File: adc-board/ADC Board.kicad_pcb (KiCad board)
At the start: 4 copper layers, 92.7 x 83.8 mm, 123 parts, among them J1 BHR-44-HUA, J10 BootJumper, J11 USB Header, J2 ST-LINK/V2, J3 USART3, J4 USART1, J5 UE27AC5410H, J6 54601-908WPLF, J7 AltPowerInput, J8 USBPowerJumper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

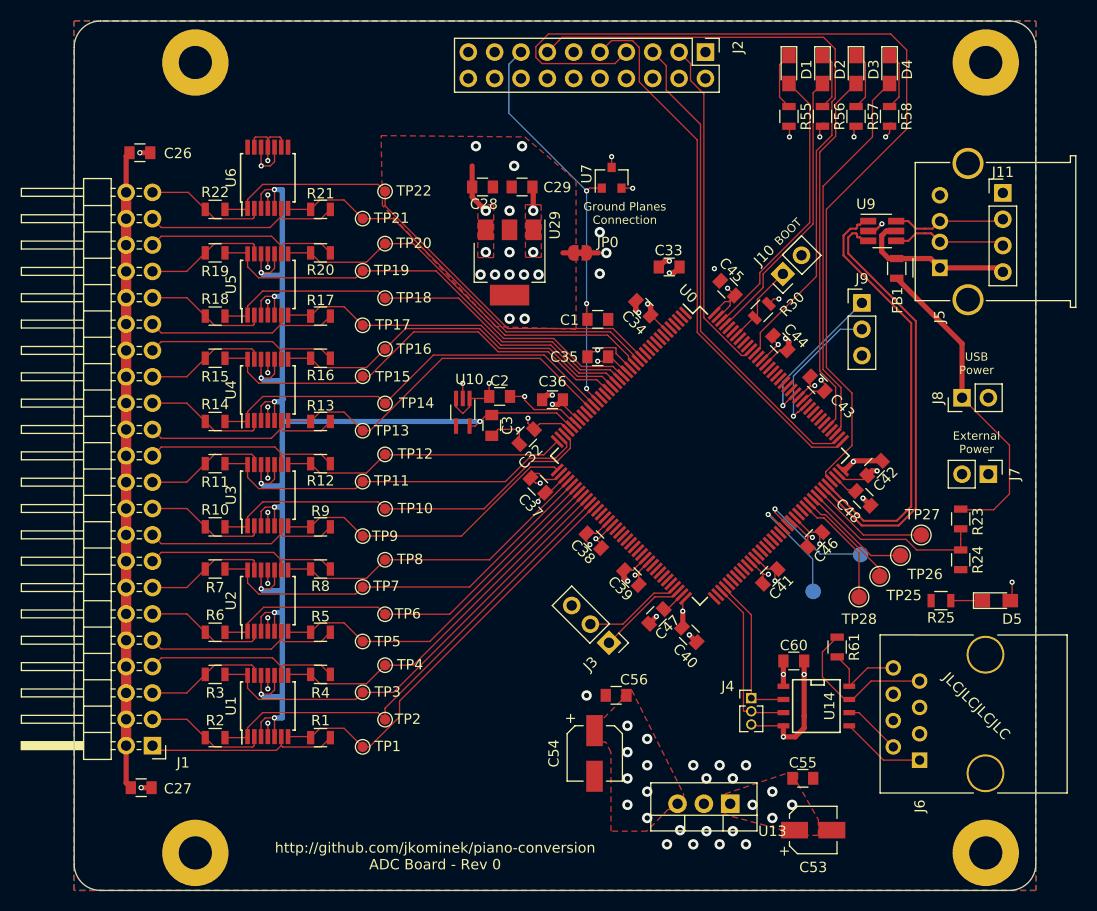
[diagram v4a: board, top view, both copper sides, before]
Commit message: Swap USART1 and USART3 on RS485 connection, so that main board has bootloader access.
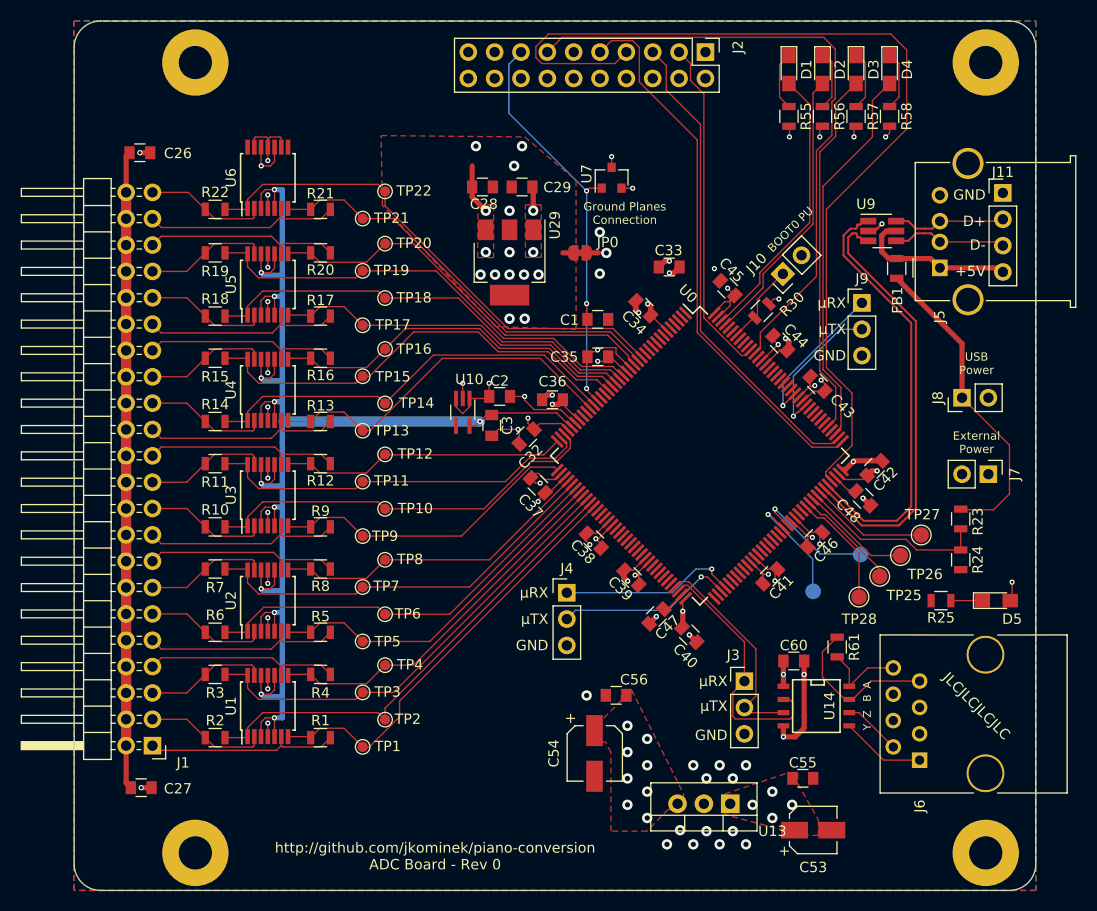
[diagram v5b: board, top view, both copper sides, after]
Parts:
- J4: footprint Pin_Headers:Pin_Header_Straight_1x03_Pitch1.27mm -> Pin_Headers:Pin_Header_Straight_1x03_Pitch2.54mm
- moved J4 20.5 mm to (79.2, 102.1)
- moved J3 13.6 mm to (96.4, 110.6), turned to 0 degrees
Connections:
- U14 pad 2: /USART1_RX -> /USART3_RX
- U14 pad 3: /USART1_TX -> /USART3_TX
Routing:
- net /USART3_RX: track 8.74 -> 24.9 mm
- net /USART3_TX: track 9.59 -> 20.8 mm
- net GNDD: track 67.0 -> 63.9 mm
- net /USART1_RX: track 15.0 -> 17.4 mm, vias 0 -> 1
- net /USART1_TX: track 16.3 -> 17.2 mm, vias 0 -> 1
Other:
- board text added: "+5V"
- board text added: "A"
- board text added: "B"
- board text added: "BOOT0 PU"
- board text added: "D+"
- board text added: "D-"
- board text added: "GND"
- board text added: "Y"
- board text added: "Z"
- board text added: "μRX"
- board text added: "μTX"
- board text removed: "BOOT"

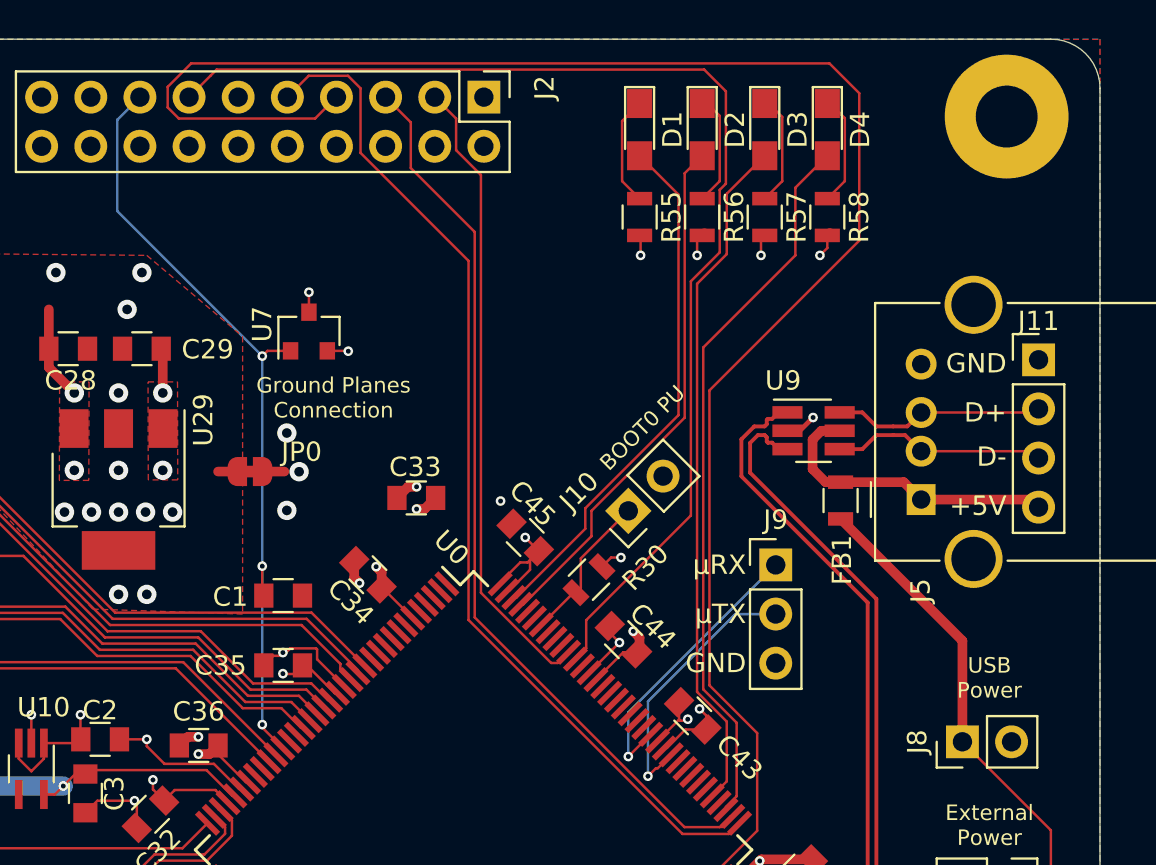
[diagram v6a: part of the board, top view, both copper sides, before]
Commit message: Tweak some copper pour boundaries and trace routing.
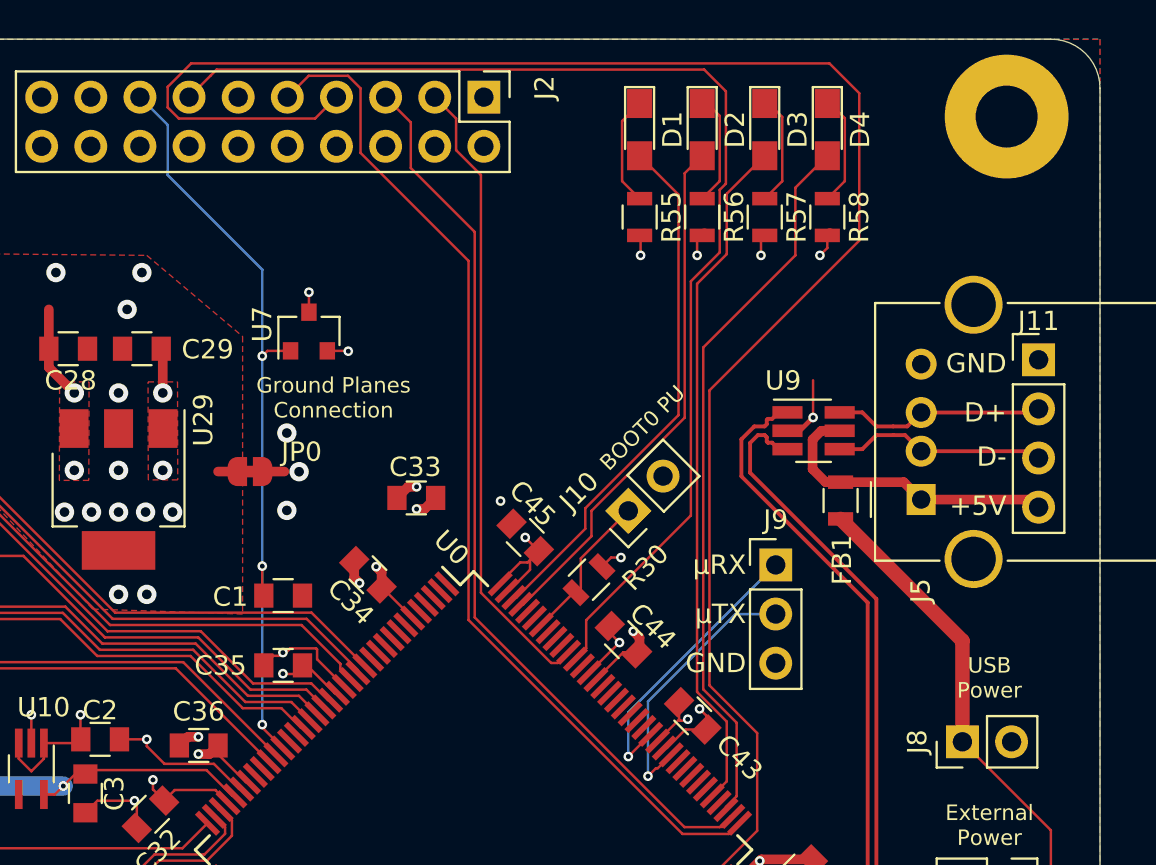
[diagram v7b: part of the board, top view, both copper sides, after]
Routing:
- net GNDD: track 63.9 -> 66.1 mm
- net /NRST: track 40.8 -> 39.8 mm

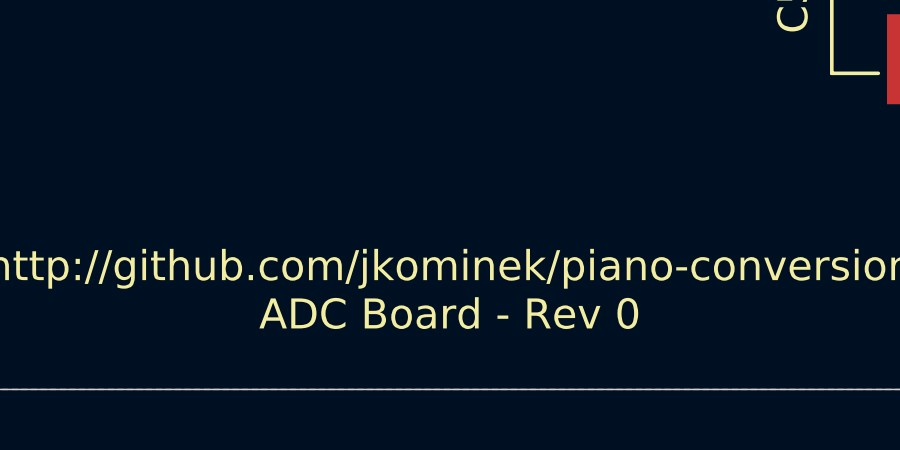
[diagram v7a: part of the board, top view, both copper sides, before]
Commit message: Add/update board rev silkscreen, nothing else
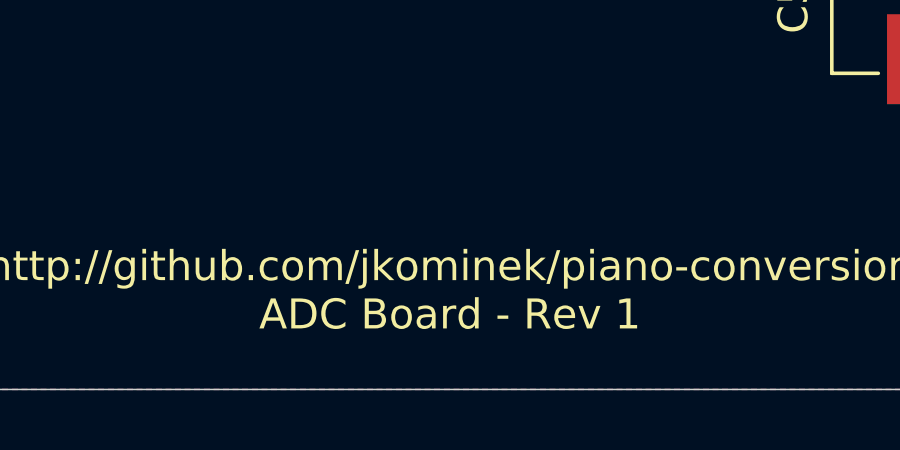
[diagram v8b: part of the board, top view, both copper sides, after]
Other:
- board text added: "http://github.com/jkominek/piano-conversion ADC Board - Rev 1"
- board text removed: "http://github.com/jkominek/piano-conversion ADC Board - Rev 0"
